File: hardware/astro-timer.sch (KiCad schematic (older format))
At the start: 25 parts, among them J1 AVR-ISP-6, J2 AudioJack3, Q1 Q_NPN_BEC, Q2 Q_NPN_BEC, SW1 SW_SPST, SW2 SW_Push, SW3 SW_Push, SW4 Rotary_Encoder_Switch, U1 ATmega328P-AU, Y1 Crystal

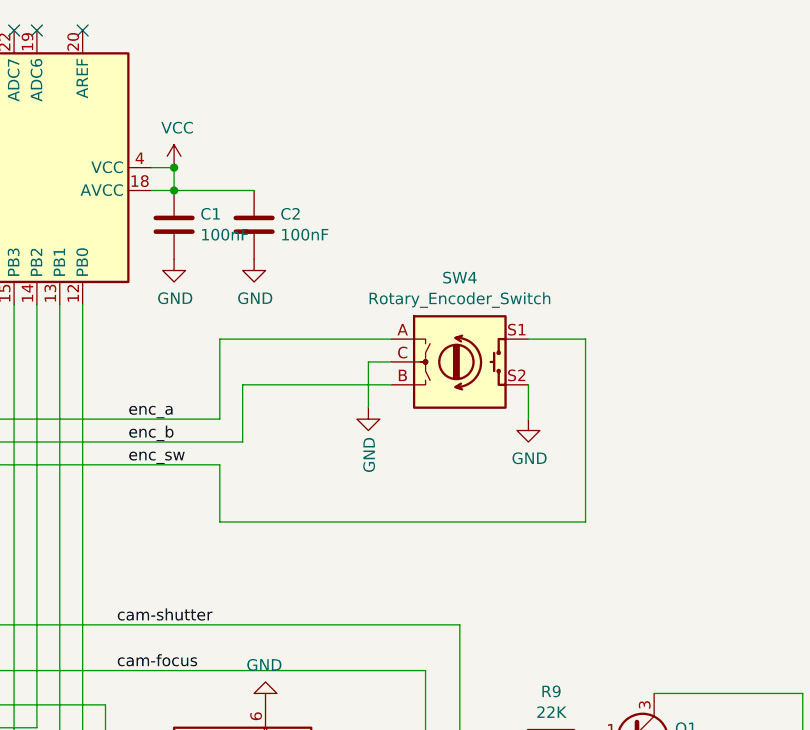
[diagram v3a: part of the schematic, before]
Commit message: add RC filter circuit for rotary encoder
seems to work pretty well on a breadboard anyway
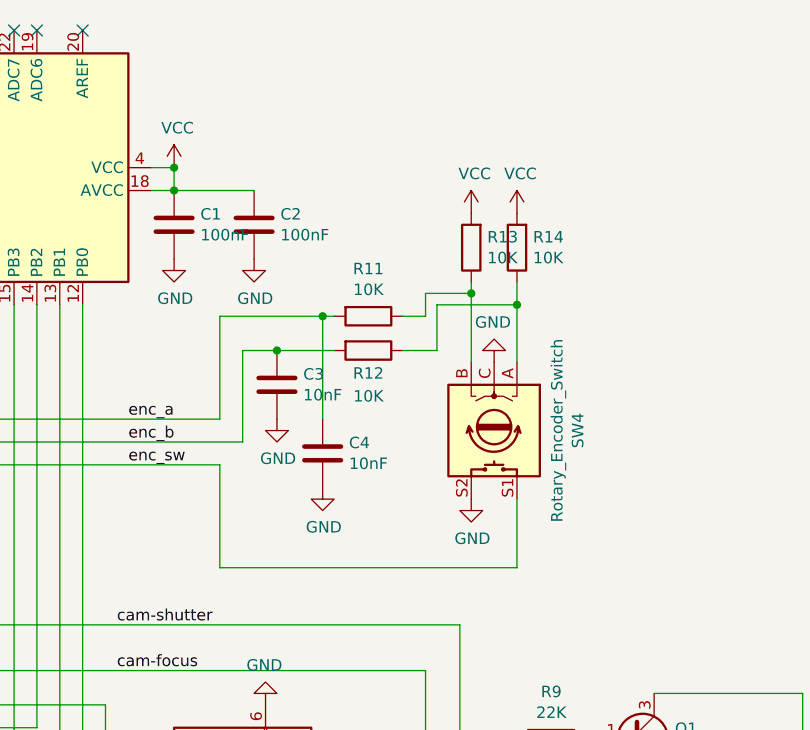
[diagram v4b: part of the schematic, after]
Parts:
- added C3, C4: 10nF, Capacitor_SMD:C_0805_2012Metric, symbol Device:C
- added R11, R12, R13, R14: 10K, Resistor_SMD:R_0805_2012Metric, symbol Device:R
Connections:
- net GND: now also C3.2, C4.2
- net VCC: now also R13.2, R14.2
- net enc_a: now also C4.1, R11.2; no longer SW4.A
- net enc_b: now also C3.1, R12.2; no longer SW4.B
- new net: R12.1, R14.1, SW4.A
- new net: R11.1, R13.1, SW4.B
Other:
- moved on the sheet: SW4
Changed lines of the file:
@@
 L power:GND #PWR011
 U 1 1 60408112
-P 7750 3050
-F 0 "#PWR011" H 7750 2800 50  0001 C CNN
-F 1 "GND" H 7755 2877 50  0000 C CNN
-F 2 "" H 7750 3050 50  0001 C CNN
-F 3 "" H 7750 3050 50  0001 C CNN
-	1    7750 3050
-	1    0    0    -1
-$EndComp
-$Comp
-L power:GND #PWR010
-U 1 1 60431874
-P 7050 3000
-F 0 "#PWR010" H 7050 2750 50  0001 C CNN
-F 1 "GND" V 7055 2872 50  0000 R CNN
-F 2 "" H 7050 3000 50  0001 C CNN
-F 3 "" H 7050 3000 50  0001 C CNN
-	1    7050 3000
-	1    0    0    -1
-$EndComp
-Wire Wire Line
-	6400 3050 6400 2700
-Wire Wire Line
-	6400 2700 7150 2700
-Wire Wire Line
-	7150 2900 6500 2900
-Wire Wire Line
-	6500 2900 6500 3150
+P 7500 3400
+F 0 "#PWR011" H 7500 3150 50  0001 C CNN
+F 1 "GND" H 7505 3227 50  0000 C CNN
+F 2 "" H 7500 3400 50  0001 C CNN
+F 3 "" H 7500 3400 50  0001 C CNN
+	1    7500 3400
+	1    0    0    -1
+$EndComp
+Wire Wire Line
+	6400 3050 6400 2600
+Wire Wire Line
+	6500 2750 6500 3150
 Wire Wire Line
 	4800 3150 6500 3150
@@
 	2150 1300 2250 1300
 Wire Wire Line
-	7750 2700 8000 2700
-Wire Wire Line
-	8000 2700 8000 3500
-Wire Wire Line
-	8000 3500 6400 3500
-Wire Wire Line
-	6400 3500 6400 3250
-Wire Wire Line
-	7150 2800 7050 2800
-Wire Wire Line
-	7050 2800 7050 3000
-Wire Wire Line
-	7750 2900 7750 3050
+	6400 3700 6400 3250
 $Comp
 L Device:Rotary_Encoder_Switch SW4
 U 1 1 6041992A
-P 7450 2800
-F 0 "SW4" H 7450 3167 50  0000 C CNN
-F 1 "Rotary_Encoder_Switch" H 7450 3076 50  0000 C CNN
-F 2 "en11:EN11HSM1AF15" H 7300 2960 50  0001 C CNN
-F 3 "~" H 7450 3060 50  0001 C CNN
-	1    7450 2800
-	1    0    0    -1
+P 7600 3100
+F 0 "SW4" H 7600 3467 50  0000 C CNN
+F 1 "Rotary_Encoder_Switch" H 7600 3376 50  0000 C CNN
+F 2 "en11:EN11HSM1AF15" H 7450 3260 50  0001 C CNN
+F 3 "~" H 7600 3360 50  0001 C CNN
+	1    7600 3100
+	0    1    1    0
 $EndComp
 $Comp
@@
 	1    0    0    -1
 $EndComp
+$Comp
+L Device:R R11
+U 1 1 604FB125
+P 7050 2600
+F 0 "R11" V 6843 2600 50  0000 C CNN
+F 1 "10K" V 6934 2600 50  0000 C CNN
+F 2 "Resistor_SMD:R_0805_2012Metric" V 6980 2600 50  0001 C CNN
+F 3 "~" H 7050 2600 50  0001 C CNN
+F 4 "C17414" V 7050 2600 50  0001 C CNN "JLC"
+	1    7050 2600
+	0    1    1    0
+$EndComp
+$Comp
+L Device:R R12
+U 1 1 604FB58C
+P 7050 2750
+F 0 "R12" V 7150 2750 50  0000 C CNN
+F 1 "10K" V 7250 2750 50  0000 C CNN
+F 2 "Resistor_SMD:R_0805_2012Metric" V 6980 2750 50  0001 C CNN
+F 3 "~" H 7050 2750 50  0001 C CNN
+F 4 "C17414" V 7050 2750 50  0001 C CNN "JLC"
+	1    7050 2750
+	0    1    1    0
+$EndComp
+$Comp
+L Device:R R13
+U 1 1 604FB812
+P 7500 2300
+F 0 "R13" H 7430 2254 50  0000 R CNN
+F 1 "10K" H 7430 2345 50  0000 R CNN
+F 2 "Resistor_SMD:R_0805_2012Metric" V 7430 2300 50  0001 C CNN
+F 3 "~" H 7500 2300 50  0001 C CNN
+F 4 "C17414" H 7500 2300 50  0001 C CNN "JLC"
+	1    7500 2300
+	-1   0    0    1
+$EndComp
+Wire Wire Line
+	6900 2750 6650 2750
+Wire Wire Line
+	6900 2600 6850 2600
+$Comp
+L Device:R R14
+U 1 1 604FC49A
+P 7700 2300
+F 0 "R14" H 7630 2254 50  0000 R CNN
+F 1 "10K" H 7630 2345 50  0000 R CNN
+F 2 "Resistor_SMD:R_0805_2012Metric" V 7630 2300 50  0001 C CNN
+F 3 "~" H 7700 2300 50  0001 C CNN
+F 4 "C17414" H 7700 2300 50  0001 C CNN "JLC"
+	1    7700 2300
+	-1   0    0    1
+$EndComp
+$Comp
+L power:VCC #PWR016
+U 1 1 60521C1F
+P 7700 2150
+F 0 "#PWR016" H 7700 2000 50  0001 C CNN
+F 1 "VCC" H 7715 2323 50  0000 C CNN
+F 2 "" H 7700 2150 50  0001 C CNN
+F 3 "" H 7700 2150 50  0001 C CNN
+	1    7700 2150
+	1    0    0    -1
+$EndComp
+$Comp
+L power:VCC #PWR014
+U 1 1 6052214C
+P 7500 2150
+F 0 "#PWR014" H 7500 2000 50  0001 C CNN
+F 1 "VCC" H 7515 2323 50  0000 C CNN
+F 2 "" H 7500 2150 50  0001 C CNN
+F 3 "" H 7500 2150 50  0001 C CNN
+	1    7500 2150
+	1    0    0    -1
+$EndComp
+Wire Wire Line
+	7700 3700 7700 3400
+Wire Wire Line
+	6400 3700 7700 3700
+Wire Wire Line
+	7700 2450 7700 2550
+Wire Wire Line
+	7500 2450 7500 2500
+$Comp
+L power:GND #PWR015
+U 1 1 6055082A
+P 7600 2800
+F 0 "#PWR015" H 7600 2550 50  0001 C CNN
+F 1 "GND" H 7605 2627 50  0000 C CNN
+F 2 "" H 7600 2800 50  0001 C CNN
+F 3 "" H 7600 2800 50  0001 C CNN
+	1    7600 2800
+	-1   0    0    1
+$EndComp
+Wire Wire Line
+	7200 2600 7300 2600
+Wire Wire Line
+	7300 2600 7300 2500
+Wire Wire Line
+	7300 2500 7500 2500
+Connection ~ 7500 2500
+Wire Wire Line
+	7500 2500 7500 2800
+Wire Wire Line
+	7200 2750 7350 2750
+Wire Wire Line
+	7350 2750 7350 2550
+Wire Wire Line
+	7350 2550 7700 2550
+Connection ~ 7700 2550
+Wire Wire Line
+	7700 2550 7700 2800
+$Comp
+L Device:C C3
+U 1 1 60568FA6
+P 6650 2900
+F 0 "C3" H 6765 2946 50  0000 L CNN
+F 1 "10nF" H 6765 2855 50  0000 L CNN
+F 2 "Capacitor_SMD:C_0805_2012Metric" H 6688 2750 50  0001 C CNN
+F 3 "~" H 6650 2900 50  0001 C CNN
+F 4 "C1710" H 6650 2900 50  0001 C CNN "JLC"
+	1    6650 2900
+	1    0    0    -1
+$EndComp
+Connection ~ 6650 2750
+Wire Wire Line
+	6650 2750 6500 2750
+$Comp
+L Device:C C4
+U 1 1 60569A85
+P 6850 3200
+F 0 "C4" H 6965 3246 50  0000 L CNN
+F 1 "10nF" H 6965 3155 50  0000 L CNN
+F 2 "Capacitor_SMD:C_0805_2012Metric" H 6888 3050 50  0001 C CNN
+F 3 "~" H 6850 3200 50  0001 C CNN
+F 4 "C1710" H 6850 3200 50  0001 C CNN "JLC"
+	1    6850 3200
+	1    0    0    -1
+$EndComp
+Wire Wire Line
+	6850 3050 6850 2600
+Connection ~ 6850 2600
+Wire Wire Line
+	6850 2600 6400 2600
+$Comp
+L power:GND #PWR013
+U 1 1 6056D312
+P 6850 3350
+F 0 "#PWR013" H 6850 3100 50  0001 C CNN
+F 1 "GND" H 6855 3177 50  0000 C CNN
+F 2 "" H 6850 3350 50  0001 C CNN
+F 3 "" H 6850 3350 50  0001 C CNN
+	1    6850 3350
+	1    0    0    -1
+$EndComp
+$Comp
+L power:GND #PWR010
+U 1 1 6056D73C
+P 6650 3050
+F 0 "#PWR010" H 6650 2800 50  0001 C CNN
+F 1 "GND" H 6655 2877 50  0000 C CNN
+F 2 "" H 6650 3050 50  0001 C CNN
+F 3 "" H 6650 3050 50  0001 C CNN
+	1    6650 3050
+	1    0    0    -1
+$EndComp

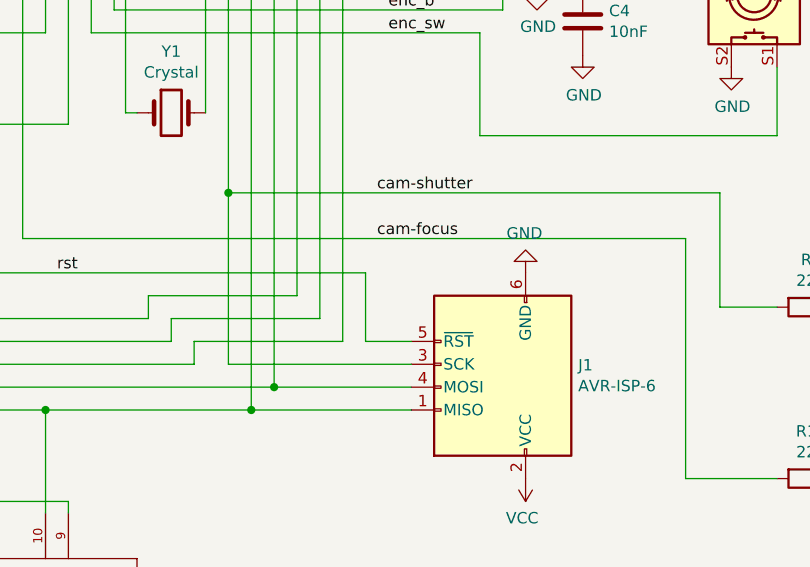
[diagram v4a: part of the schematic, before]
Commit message: add 10K external pullup on ~RESET
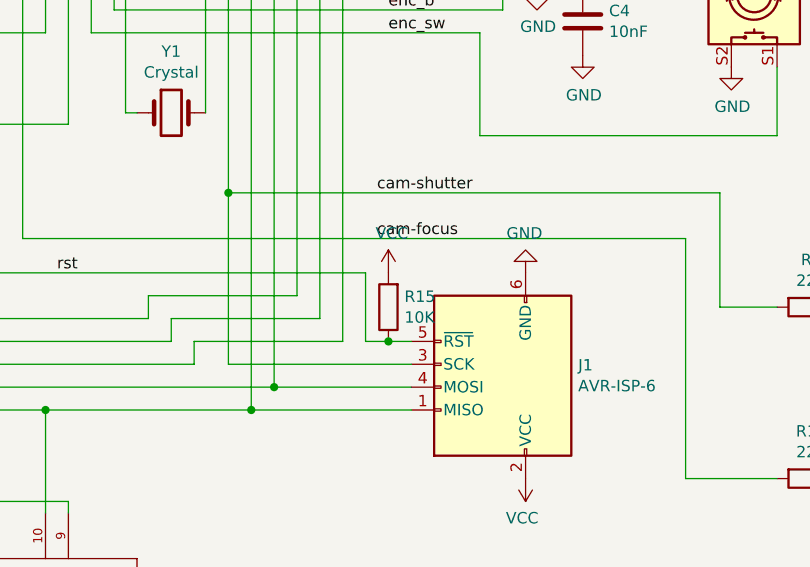
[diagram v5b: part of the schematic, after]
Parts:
- added R15: 10K, Resistor_SMD:R_0805_2012Metric, symbol Device:R
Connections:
- net VCC: now also R15.2
- net rst: now also R15.1
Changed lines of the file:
@@
 	6100 4700 5300 4700
 Wire Wire Line
-	6100 4600 5900 4600
+	6100 4600 6000 4600
 Wire Wire Line
 	5150 4700 5150 4600
@@
 	1    0    0    -1
 $EndComp
+$Comp
+L Device:R R15
+U 1 1 604FD70B
+P 6000 4450
+F 0 "R15" H 5930 4404 50  0000 R CNN
+F 1 "10K" H 5930 4495 50  0000 R CNN
+F 2 "Resistor_SMD:R_0805_2012Metric" V 5930 4450 50  0001 C CNN
+F 3 "~" H 6000 4450 50  0001 C CNN
+F 4 "C17414" H 6000 4450 50  0001 C CNN "JLC"
+	1    6000 4450
+	-1   0    0    1
+$EndComp
+Connection ~ 6000 4600
+Wire Wire Line
+	6000 4600 5900 4600
+$Comp
+L power:VCC #PWR017
+U 1 1 604FE3F2
+P 6000 4300
+F 0 "#PWR017" H 6000 4150 50  0001 C CNN
+F 1 "VCC" H 6015 4473 50  0000 C CNN
+F 2 "" H 6000 4300 50  0001 C CNN
+F 3 "" H 6000 4300 50  0001 C CNN
+	1    6000 4300
+	1    0    0    -1
+$EndComp

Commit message: use more common 0603 package for low-current resistors
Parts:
- Q1, Q2: JLC C6749 -> C2146
- R10, R9: footprint Resistor_SMD:R_0805_2012Metric -> Resistor_SMD:R_0603_1608Metric; JLC C17560 -> C31850
- R11, R12, R13, R14, R15: footprint Resistor_SMD:R_0805_2012Metric -> Resistor_SMD:R_0603_1608Metric; JLC C17414 -> C25804
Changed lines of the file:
@@
 F 0 "R9" V 7643 4450 50  0000 C CNN
 F 1 "22K" V 7734 4450 50  0000 C CNN
-F 2 "Resistor_SMD:R_0805_2012Metric" V 7780 4450 50  0001 C CNN
+F 2 "Resistor_SMD:R_0603_1608Metric" V 7780 4450 50  0001 C CNN
 F 3 "~" H 7850 4450 50  0001 C CNN
-F 4 "C17560" V 7850 4450 50  0001 C CNN "JLC"
+F 4 "C31850" V 7850 4450 50  0001 C CNN "JLC"
 	1    7850 4450
 	0    1    1    0
@@
 F 0 "R10" V 7643 5200 50  0000 C CNN
 F 1 "22K" V 7734 5200 50  0000 C CNN
-F 2 "Resistor_SMD:R_0805_2012Metric" V 7780 5200 50  0001 C CNN
+F 2 "Resistor_SMD:R_0603_1608Metric" V 7780 5200 50  0001 C CNN
 F 3 "~" H 7850 5200 50  0001 C CNN
-F 4 "C17560" V 7850 5200 50  0001 C CNN "JLC"
+F 4 "C31850" V 7850 5200 50  0001 C CNN "JLC"
 	1    7850 5200
 	0    1    1    0
@@
 F 2 "Package_TO_SOT_SMD:SOT-23" H 8400 4550 50  0001 C CNN
 F 3 "~" H 8200 4450 50  0001 C CNN
-F 4 "C6749" H 8200 4450 50  0001 C CNN "JLC"
+F 4 "C2146" H 8200 4450 50  0001 C CNN "JLC"
 	1    8200 4450
 	1    0    0    -1
@@
 F 2 "Package_TO_SOT_SMD:SOT-23" H 8400 5300 50  0001 C CNN
 F 3 "~" H 8200 5200 50  0001 C CNN
-F 4 "C6749" H 8200 5200 50  0001 C CNN "JLC"
+F 4 "C2146" H 8200 5200 50  0001 C CNN "JLC"
 	1    8200 5200
 	1    0    0    -1
@@
 F 0 "R11" V 6843 2600 50  0000 C CNN
 F 1 "10K" V 6934 2600 50  0000 C CNN
-F 2 "Resistor_SMD:R_0805_2012Metric" V 6980 2600 50  0001 C CNN
+F 2 "Resistor_SMD:R_0603_1608Metric" V 6980 2600 50  0001 C CNN
 F 3 "~" H 7050 2600 50  0001 C CNN
-F 4 "C17414" V 7050 2600 50  0001 C CNN "JLC"
+F 4 "C25804" V 7050 2600 50  0001 C CNN "JLC"
 	1    7050 2600
 	0    1    1    0
@@
 F 0 "R12" V 7150 2750 50  0000 C CNN
 F 1 "10K" V 7250 2750 50  0000 C CNN
-F 2 "Resistor_SMD:R_0805_2012Metric" V 6980 2750 50  0001 C CNN
+F 2 "Resistor_SMD:R_0603_1608Metric" V 6980 2750 50  0001 C CNN
 F 3 "~" H 7050 2750 50  0001 C CNN
-F 4 "C17414" V 7050 2750 50  0001 C CNN "JLC"
+F 4 "C25804" V 7050 2750 50  0001 C CNN "JLC"
 	1    7050 2750
 	0    1    1    0
@@
 F 0 "R13" H 7430 2254 50  0000 R CNN
 F 1 "10K" H 7430 2345 50  0000 R CNN
-F 2 "Resistor_SMD:R_0805_2012Metric" V 7430 2300 50  0001 C CNN
+F 2 "Resistor_SMD:R_0603_1608Metric" V 7430 2300 50  0001 C CNN
 F 3 "~" H 7500 2300 50  0001 C CNN
-F 4 "C17414" H 7500 2300 50  0001 C CNN "JLC"
+F 4 "C25804" H 7500 2300 50  0001 C CNN "JLC"
 	1    7500 2300
 	-1   0    0    1
@@
 F 0 "R14" H 7630 2254 50  0000 R CNN
 F 1 "10K" H 7630 2345 50  0000 R CNN
-F 2 "Resistor_SMD:R_0805_2012Metric" V 7630 2300 50  0001 C CNN
+F 2 "Resistor_SMD:R_0603_1608Metric" V 7630 2300 50  0001 C CNN
 F 3 "~" H 7700 2300 50  0001 C CNN
-F 4 "C17414" H 7700 2300 50  0001 C CNN "JLC"
+F 4 "C25804" H 7700 2300 50  0001 C CNN "JLC"
 	1    7700 2300
 	-1   0    0    1
@@
 F 0 "R15" H 5930 4404 50  0000 R CNN
 F 1 "10K" H 5930 4495 50  0000 R CNN
-F 2 "Resistor_SMD:R_0805_2012Metric" V 5930 4450 50  0001 C CNN
+F 2 "Resistor_SMD:R_0603_1608Metric" V 5930 4450 50  0001 C CNN
 F 3 "~" H 6000 4450 50  0001 C CNN
-F 4 "C17414" H 6000 4450 50  0001 C CNN "JLC"
+F 4 "C25804" H 6000 4450 50  0001 C CNN "JLC"
 	1    6000 4450
 	-1   0    0    1

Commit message: one inch tall
honestly, I did this for the challenge and I will probably
not get this fabricated :P
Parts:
- removed BT1, BT2: Battery_Cell, sparkfun-batteries:BATTERY-AAA, symbol sparkfun-batts:BATTERY-AAA
- removed C2: 100nF, Capacitor_SMD:C_0805_2012Metric, symbol Device:C
- removed SW1: SW_SPST, digikey:Switch_Slide_11.6x4mm_EG1218, symbol Switch:SW_SPST
- added BT1: Battery, Connector_PinHeader_2.54mm:PinHeader_1x02_P2.54mm_Horizontal, symbol Device:Battery
- SW4: footprint en11:EN11HSM1AF15 -> more_different_en11:EN11-VSM1AF20
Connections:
- net GND: now also BT1.2 (-)
- net VCC: now also BT1.1 (+)
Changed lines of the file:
@@
 L power:GND #PWR01
 U 1 1 60349228
-P 1750 2200
-F 0 "#PWR01" H 1750 1950 50  0001 C CNN
-F 1 "GND" H 1755 2027 50  0000 C CNN
-F 2 "" H 1750 2200 50  0001 C CNN
-F 3 "" H 1750 2200 50  0001 C CNN
-	1    1750 2200
+P 1750 1850
+F 0 "#PWR01" H 1750 1600 50  0001 C CNN
+F 1 "GND" H 1755 1677 50  0000 C CNN
+F 2 "" H 1750 1850 50  0001 C CNN
+F 3 "" H 1750 1850 50  0001 C CNN
+	1    1750 1850
 	1    0    0    -1
 $EndComp
@@
 L power:VCC #PWR02
 U 1 1 60348A56
-P 2250 1300
-F 0 "#PWR02" H 2250 1150 50  0001 C CNN
-F 1 "VCC" H 2265 1473 50  0000 C CNN
-F 2 "" H 2250 1300 50  0001 C CNN
-F 3 "" H 2250 1300 50  0001 C CNN
-	1    2250 1300
-	1    0    0    -1
-$EndComp
-$Comp
-L sparkfun-batts:BATTERY-AAA BT2
-U 1 1 603EB8A6
-P 1750 2000
-F 0 "BT2" V 1700 2200 50  0000 L CNN
-F 1 "Battery_Cell" V 1800 2200 50  0000 L CNN
-F 2 "sparkfun-batteries:BATTERY-AAA" V 1750 2060 50  0001 C CNN
-F 3 "~" V 1750 2060 50  0001 C CNN
-	1    1750 2000
-	0    1    1    0
-$EndComp
-$Comp
-L sparkfun-batts:BATTERY-AAA BT1
-U 1 1 603EBBDC
-P 1750 1600
-F 0 "BT1" V 1700 1800 50  0000 L CNN
-F 1 "Battery_Cell" V 1800 1800 50  0000 L CNN
-F 2 "sparkfun-batteries:BATTERY-AAA" V 1750 1660 50  0001 C CNN
-F 3 "~" V 1750 1660 50  0001 C CNN
-	1    1750 1600
-	0    1    1    0
+P 1750 1300
+F 0 "#PWR02" H 1750 1150 50  0001 C CNN
+F 1 "VCC" H 1765 1473 50  0000 C CNN
+F 2 "" H 1750 1300 50  0001 C CNN
+F 3 "" H 1750 1300 50  0001 C CNN
+	1    1750 1300
+	1    0    0    -1
 $EndComp
 Wire Wire Line
@@
 Text Label 4550 4300 0    50   ~ 0
 rst
-$Comp
-L Switch:SW_SPST SW1
-U 1 1 603E081C
-P 1950 1300
-F 0 "SW1" H 1950 1535 50  0000 C CNN
-F 1 "SW_SPST" H 1950 1444 50  0000 C CNN
-F 2 "digikey:Switch_Slide_11.6x4mm_EG1218" H 1950 1300 50  0001 C CNN
-F 3 "~" H 1950 1300 50  0001 C CNN
-	1    1950 1300
-	1    0    0    -1
-$EndComp
 Wire Wire Line
 	1750 1300 1750 1400
-Wire Wire Line
-	2150 1300 2250 1300
 Wire Wire Line
 	6400 3700 6400 3250
@@
 F 0 "SW4" H 7600 3467 50  0000 C CNN
 F 1 "Rotary_Encoder_Switch" H 7600 3376 50  0000 C CNN
-F 2 "en11:EN11HSM1AF15" H 7450 3260 50  0001 C CNN
+F 2 "more_different_en11:EN11-VSM1AF20" H 7450 3260 50  0001 C CNN
 F 3 "~" H 7600 3360 50  0001 C CNN
 	1    7600 3100
@@
 $EndComp
 $Comp
-L Device:C C2
-U 1 1 60556B9F
-P 6550 2200
-F 0 "C2" H 6665 2246 50  0000 L CNN
-F 1 "100nF" H 6665 2155 50  0000 L CNN
-F 2 "Capacitor_SMD:C_0805_2012Metric" H 6588 2050 50  0001 C CNN
-F 3 "~" H 6550 2200 50  0001 C CNN
-F 4 "C49678" H 6550 2200 50  0001 C CNN "JLC"
-	1    6550 2200
-	1    0    0    -1
-$EndComp
-Wire Wire Line
-	6550 2050 6200 2050
-$Comp
-L power:GND #PWR07
-U 1 1 6055A060
-P 6550 2350
-F 0 "#PWR07" H 6550 2100 50  0001 C CNN
-F 1 "GND" H 6555 2177 50  0000 C CNN
-F 2 "" H 6550 2350 50  0001 C CNN
-F 3 "" H 6550 2350 50  0001 C CNN
-	1    6550 2350
-	1    0    0    -1
-$EndComp
-$Comp
 L Device:R R11
 U 1 1 604FB125
@@
 	1    0    0    -1
 $EndComp
+Wire Wire Line
+	1750 1850 1750 1800
+$Comp
+L Device:Battery BT1
+U 1 1 605F4C57
+P 1750 1600
+F 0 "BT1" H 1858 1646 50  0000 L CNN
+F 1 "Battery" H 1858 1555 50  0000 L CNN
+F 2 "Connector_PinHeader_2.54mm:PinHeader_1x02_P2.54mm_Horizontal" V 1750 1660 50  0001 C CNN
+F 3 "~" V 1750 1660 50  0001 C CNN
+	1    1750 1600
+	1    0    0    -1
+$EndComp
